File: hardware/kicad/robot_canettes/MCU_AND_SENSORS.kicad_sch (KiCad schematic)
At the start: 26 parts, among them J1 C590562, J2 C590562, J3 C573320, U1 STM32G431RBTx, Y1 16MHz

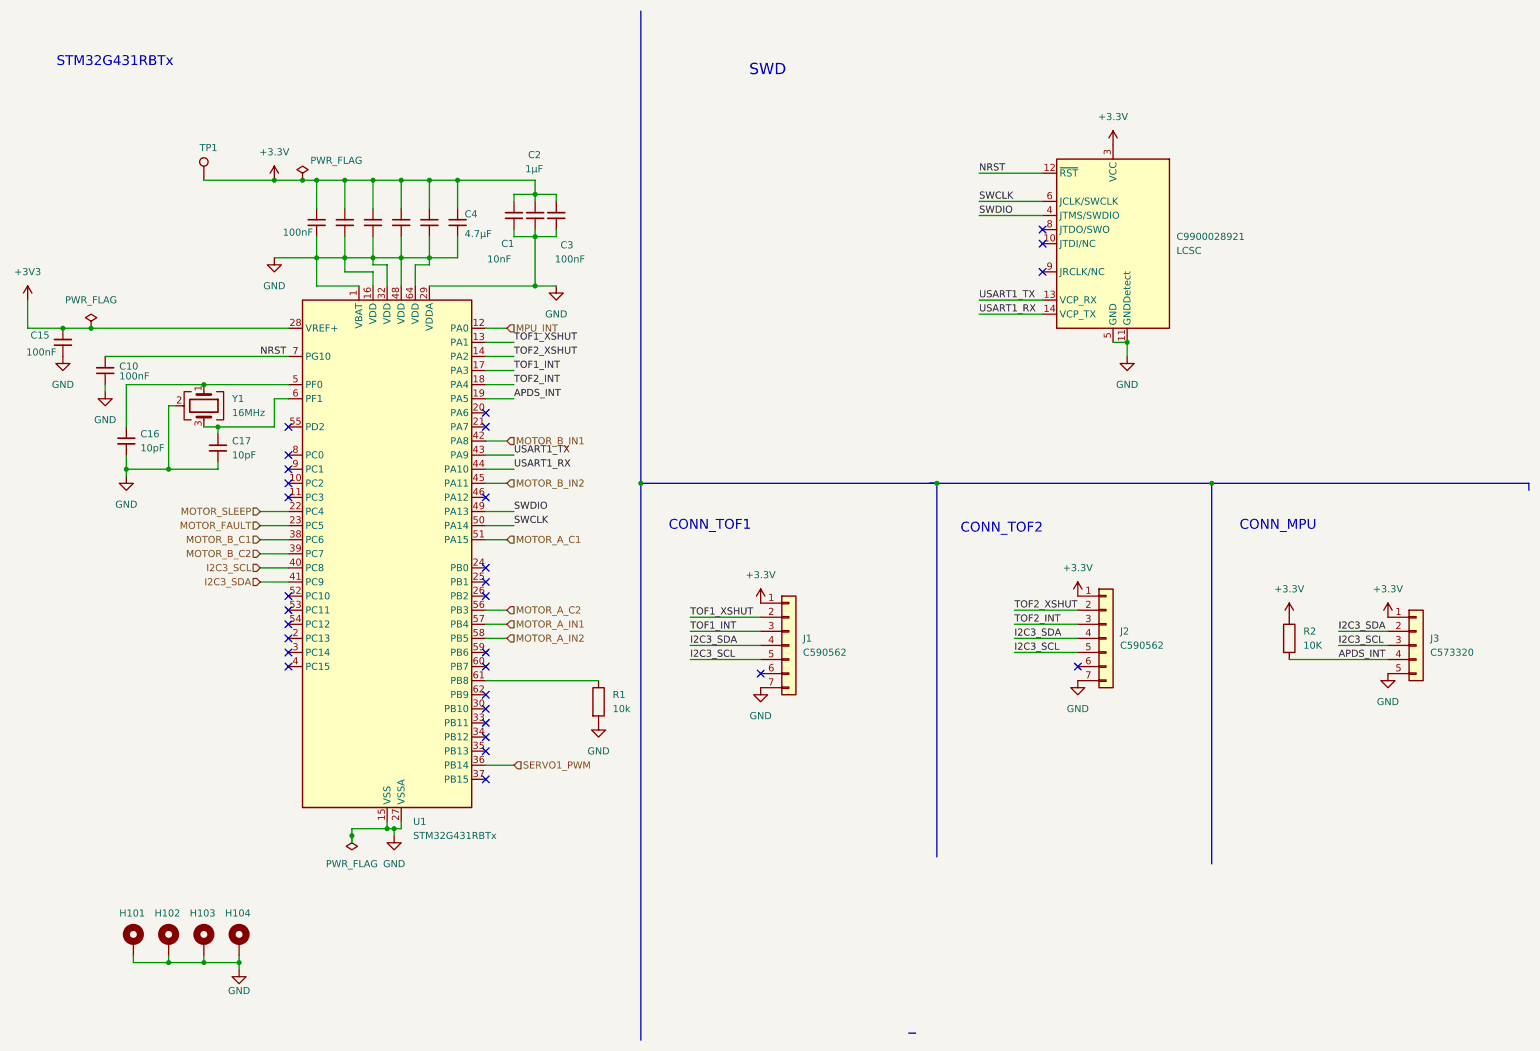
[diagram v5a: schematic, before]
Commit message: MAJ connecteur TOF2 (J10) et resistances pull-up
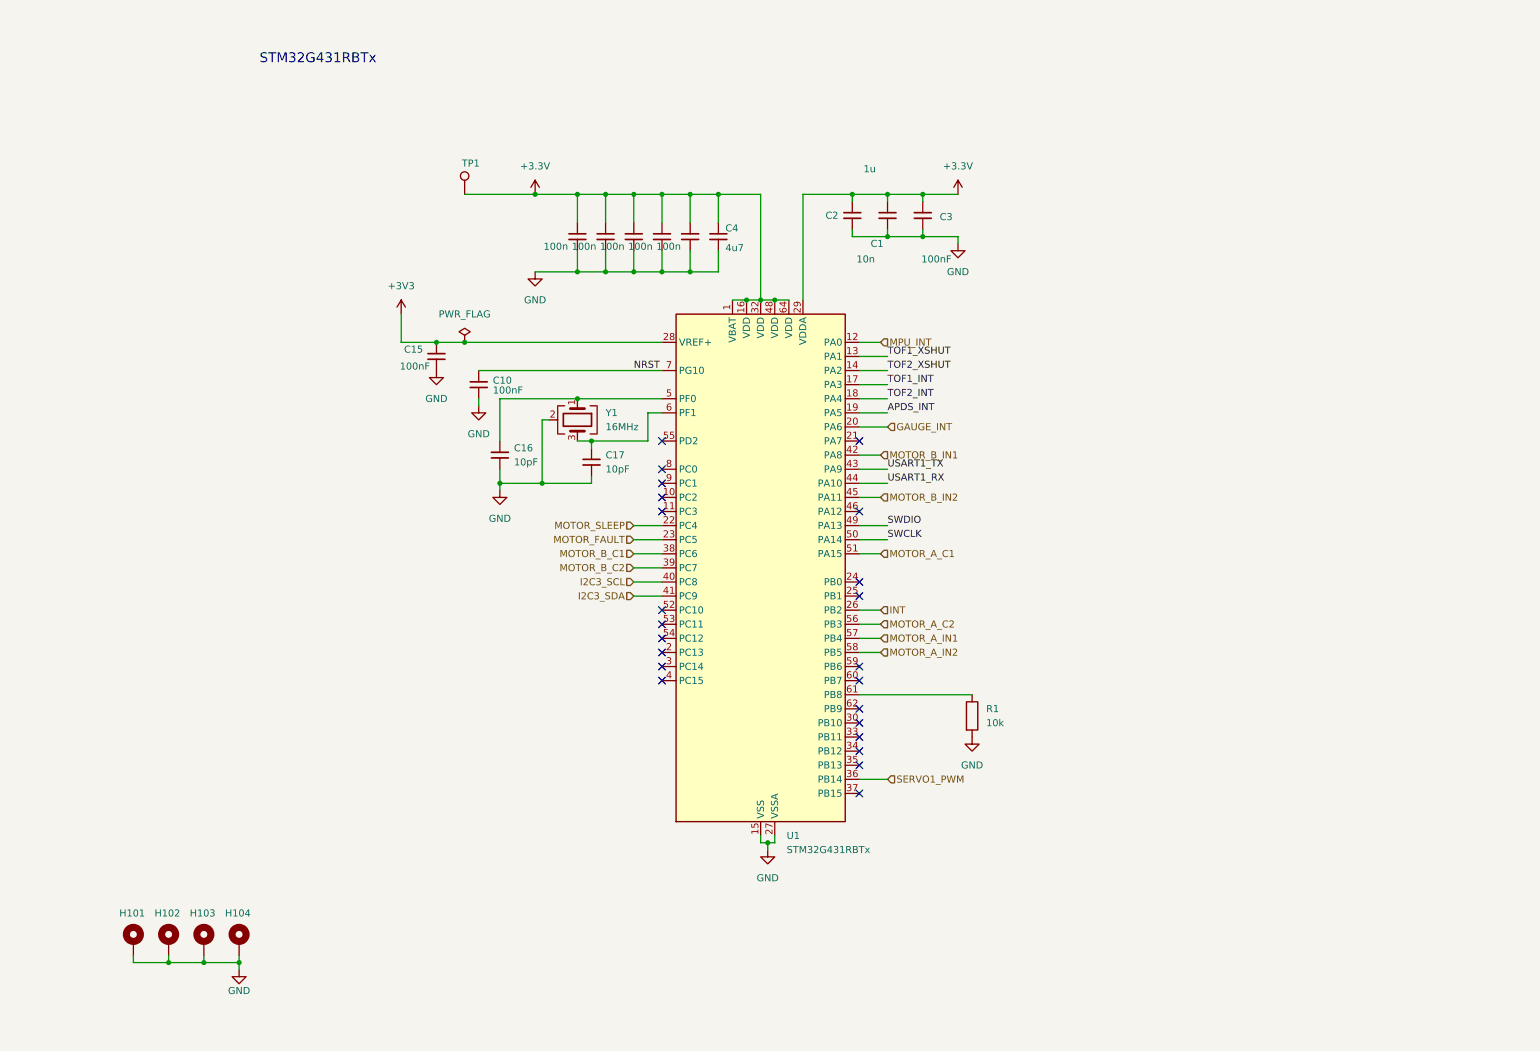
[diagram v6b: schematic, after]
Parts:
- removed J1, J2: C590562, symbol Connector_Generic:Conn_01x07
- removed J3: C573320, symbol Connector_Generic:Conn_01x05
- removed LCSC: C9900028921, Package_TO_SOT_SMD:TO-252-2, symbol Connector:Conn_ST_STDC14
- removed R2: 10K, symbol Device:R
- C1: value 10nF -> 10n
- C2: value 1µF -> 1u
- C4: value 4.7µF -> 4u7
- C5, C6, C7, C8, C9: value 100nF -> 100n
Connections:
- net +3.3V: now also U1.1 (VBAT), U1.16 (VDD), U1.29 (VDDA), U1.32 (VDD), U1.48 (VDD), U1.64 (VDD)
- net GND: no longer U1.1 (VBAT), U1.16 (VDD), U1.29 (VDDA), U1.32 (VDD), U1.48 (VDD), U1.64 (VDD)
- net GAUGE_INT: now reaches U1.20 (PA6)
- net INT: now reaches U1.26 (PB2)
- no-connect marks 30 -> 23
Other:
- note removed: "CONN_MPU"
- note removed: "CONN_TOF1"
- note removed: "CONN_TOF2"
- note removed: "SWD"
- moved on the sheet: C10, C15, C16, C17, C4, R1, TP1, U1, Y1
